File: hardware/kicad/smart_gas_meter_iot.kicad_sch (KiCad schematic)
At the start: 19 parts, among them J1 ESP32-S3-DEVKITC-1-J1, J2 ESP32-S3-DEVKITC-1-J2, J3 ESP-Prog-ProgramCOM-RECV, J4 USB2.0_C_v3, SW1 RS, SW2 BT, U1 ESP32-S3-WROOM-1, U2 AMS1117-3.3

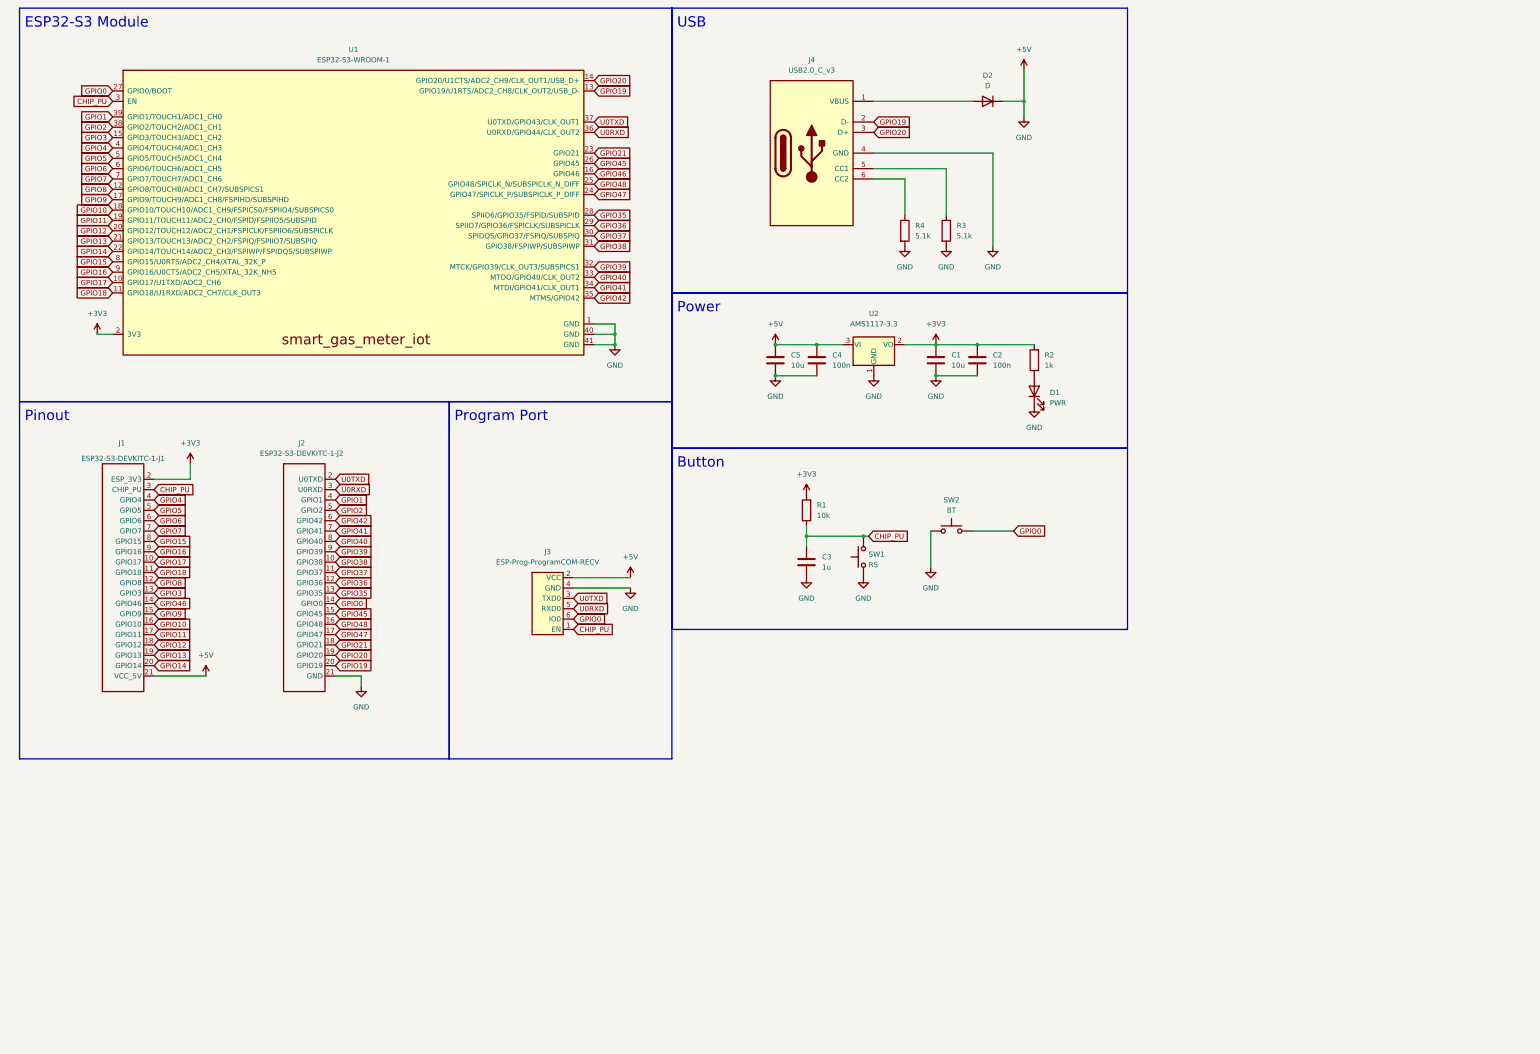
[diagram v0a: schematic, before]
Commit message: Rebuild v0.2 KiCad schematic from a reviewed design table (ERC clean)
Controlled rebuild per CONTROLLED_REBUILD_SPEC.md steps 1-5:
- Archive the frozen draft (65 ERC messages, +5V/GND short) as evidence.
- Add design_v02.py as the single source of truth (parts, values,
  footprints, pin-to-net map) and tools/generate_schematic.py to build
  the native schematic, project file and project-local SGM symbol and
  footprint libraries from it.
- Module-only carrier: USB-C with separate CC Rd, PTC + TVS, USBLC6 ESD,
  AP63203 buck (datasheet typical application), ESP32-S3-WROOM-1-N8 with
  EN RC and BOOT/RESET, synthetic pulse input on GPIO4, status LED,
  tamper input, I2C/UART headers, modem daughterboard connector with a
  separate MODEM_VIN, and test points.
- KiCad 9.0.3 ERC: 0 errors, 0 warnings, no exclusions.
- Add check_netlist_matches_design.py and run it in CAD CI together with
  a schematic/design sync check.
- Fix check_netlist_invariants.py: the net parser missed the last net and
  never read pinfunction, so GND-on-rail checks could not fire; identify
  legacy dev-board headers by library/part instead of J1/J2 refs; normalise
  local-label net names; add a modem-on-3V3 check. It now reports all 10
  faults of the archived draft.
- Export schematic PDF/PNG, ERC report, netlist and generated BOM.
- Add .gitignore; fix literal \n in README roadmaps.

Co-Authored-By: Claude Opus 5.5 <noreply@anthropic.com>
Claude-Session: https://claude.ai/code/session_01KogE8voCCVefmDU5WM67kg
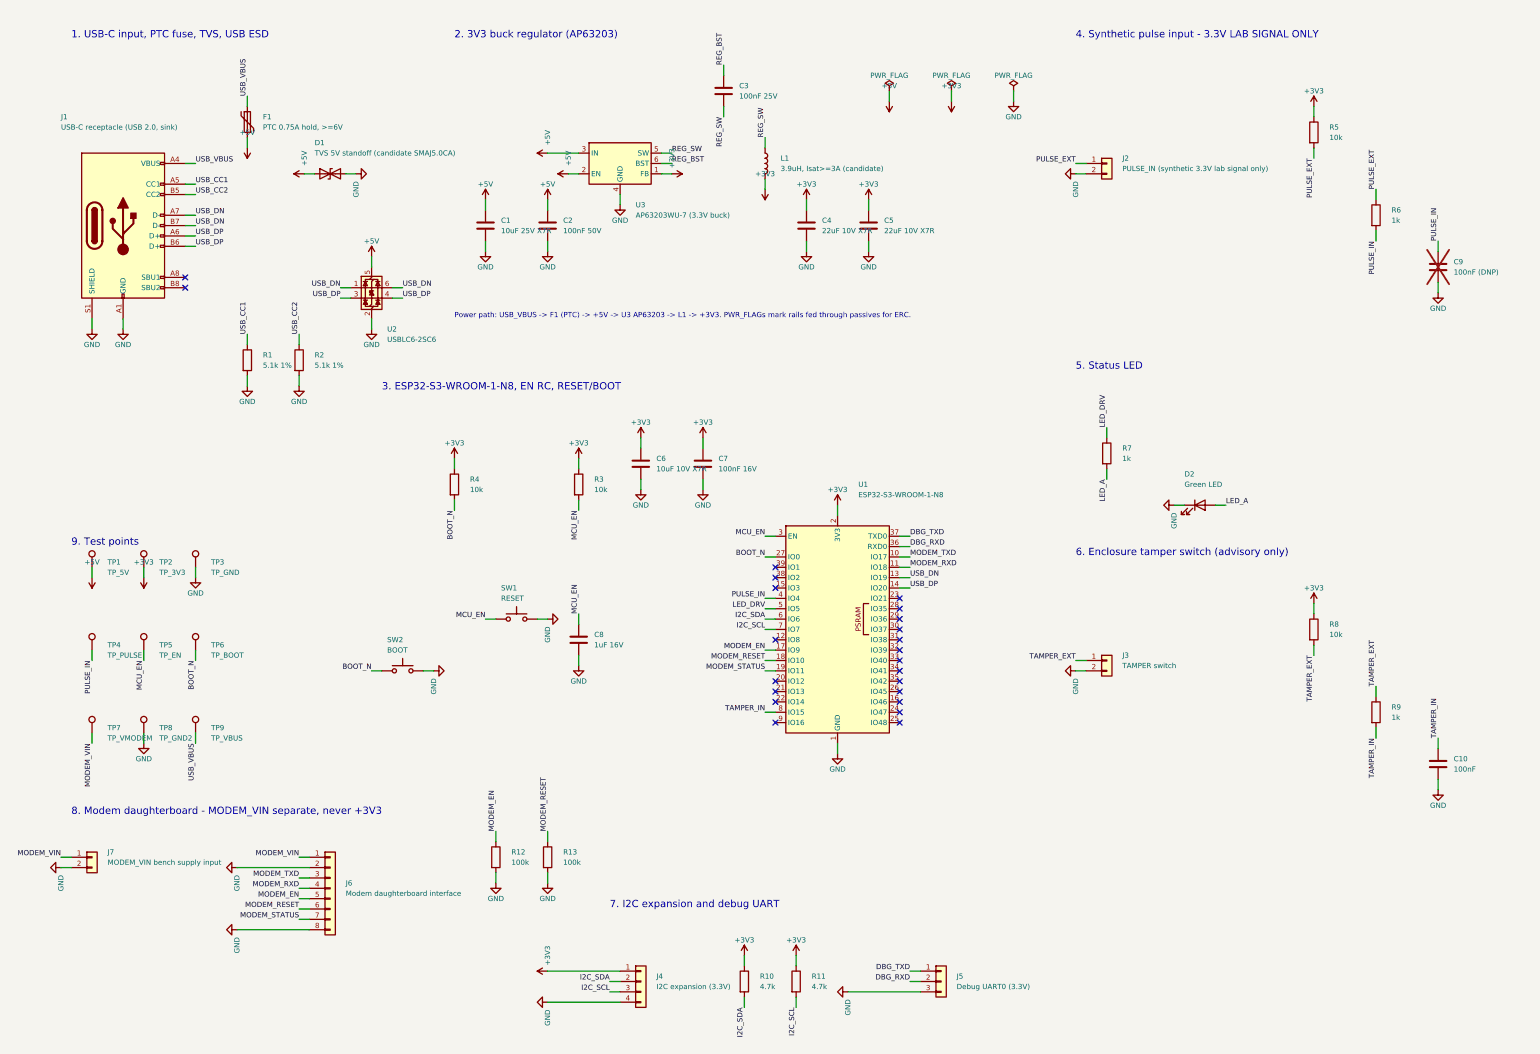
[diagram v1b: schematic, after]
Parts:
- removed C1, C5: 10u, esp32-dev-boards:Capacitor_0805_2012, symbol Device:C
- removed C2, C4: 100n, esp32-dev-boards:Capacitor_0805_2012, symbol Device:C
- removed C3: 1u, esp32-dev-boards:Capacitor_0805_2012, symbol Device:C
- removed D1: PWR, LED_SMD:LED_0805_2012Metric_Pad1.15x1.40mm_HandSolder, symbol Device:LED
- removed D2: D, Diode_SMD:D_SMA, symbol Device:D
- removed J1: ESP32-S3-DEVKITC-1-J1, esp32-dev-boards:ESP32-S3-DEVKITC-J1-mini, symbol esp32-dev-boards:ESP32-S3-DEVKITC-1-J1-mini
- removed J2: ESP32-S3-DEVKITC-1-J2, esp32-dev-boards:ESP32-S3-DEVKITC-J2-mini, symbol esp32-dev-boards:ESP32-S3-DEVKITC-1-J2-mini
- removed J3: ESP-Prog-ProgramCOM-RECV, $74th:BoxPinHeader_2x03_P1.27mm_Vertical, symbol $74th:ESP-Prog-ProgramCOM-RECV
- removed J4: USB2.0_C_v3, $74th:USB-C-12-Pin-SMD, symbol $74th:USB2.0_C_v3
- removed R1: 10k, esp32-dev-boards:Register_0805_2012, symbol Device:R
- removed R2: 1k, esp32-dev-boards:Register_0805_2012, symbol Device:R
- removed R3, R4: 5.1k, esp32-dev-boards:Register_0805_2012, symbol Device:R
- removed SW1: RS, esp32-dev-boards:SKRPABE010, symbol Switch:SW_Push
- removed SW2: BT, esp32-dev-boards:SKRPABE010, symbol Switch:SW_Push
- removed U1: ESP32-S3-WROOM-1, Espressif:ESP32-S3-WROOM-1, symbol Espressif:ESP32-S3-WROOM-1
- removed U2: AMS1117-3.3, Package_TO_SOT_SMD:SOT-223-3_TabPin2, symbol Regulator_Linear:AMS1117-3.3
- added C1: 10uF 25V X7R, SGM:C_1206_3216Metric, symbol SGM:C
- added C10: 100nF, SGM:C_0603_1608Metric, symbol SGM:C
- added C2: 100nF 50V, SGM:C_0603_1608Metric, symbol SGM:C
- added C3: 100nF 25V, SGM:C_0603_1608Metric, symbol SGM:C
- added C4, C5: 22uF 10V X7R, SGM:C_0805_2012Metric, symbol SGM:C
- added C6: 10uF 10V X7R, SGM:C_0805_2012Metric, symbol SGM:C
- added C7: 100nF 16V, SGM:C_0603_1608Metric, symbol SGM:C
- added C8: 1uF 16V, SGM:C_0603_1608Metric, symbol SGM:C
- added C9: 100nF (DNP), SGM:C_0603_1608Metric, symbol SGM:C
- added D1: TVS 5V standoff (candidate SMAJ5.0CA), SGM:D_SMA, symbol SGM:D_TVS
- added D2: Green LED, SGM:LED_0603_1608Metric, symbol SGM:LED
- added F1: PTC 0.75A hold, >=6V, SGM:Fuse_1206_3216Metric, symbol SGM:Polyfuse
- added J1: USB-C receptacle (USB 2.0, sink), SGM:USB_C_Receptacle_GCT_USB4105-xx-A_16P_TopMnt_Horizontal, symbol SGM:USB_C_Receptacle_USB2.0_16P
- added J2: PULSE_IN (synthetic 3.3V lab signal only), SGM:PinHeader_1x02_P2.54mm_Vertical, symbol SGM:Conn_01x02
- added J3: TAMPER switch, SGM:PinHeader_1x02_P2.54mm_Vertical, symbol SGM:Conn_01x02
- added J4: I2C expansion (3.3V), SGM:PinHeader_1x04_P2.54mm_Vertical, symbol SGM:Conn_01x04
- added J5: Debug UART0 (3.3V), SGM:PinHeader_1x03_P2.54mm_Vertical, symbol SGM:Conn_01x03
- added J6: Modem daughterboard interface, SGM:PinHeader_1x08_P2.54mm_Vertical, symbol SGM:Conn_01x08
- added J7: MODEM_VIN bench supply input, SGM:PinHeader_1x02_P2.54mm_Vertical, symbol SGM:Conn_01x02
- added L1: 3.9uH, Isat>=3A (candidate), SGM:L_Taiyo-Yuden_NR-40xx, symbol SGM:L
- added R1, R2: 5.1k 1%, SGM:R_0603_1608Metric, symbol SGM:R
- added R10, R11: 4.7k, SGM:R_0603_1608Metric, symbol SGM:R
- added R12, R13: 100k, SGM:R_0603_1608Metric, symbol SGM:R
- added R3, R4, R5, R8: 10k, SGM:R_0603_1608Metric, symbol SGM:R
- added R6, R7, R9: 1k, SGM:R_0603_1608Metric, symbol SGM:R
- added SW1: RESET, SGM:SW_SPST_TL3342, symbol SGM:SW_Push
- added SW2: BOOT, SGM:SW_SPST_TL3342, symbol SGM:SW_Push
- added TP1: TP_5V, SGM:TestPoint_Pad_D1.5mm, symbol SGM:TestPoint
- added TP2: TP_3V3, SGM:TestPoint_Pad_D1.5mm, symbol SGM:TestPoint
- added TP3: TP_GND, SGM:TestPoint_Pad_D1.5mm, symbol SGM:TestPoint
- added TP4: TP_PULSE, SGM:TestPoint_Pad_D1.5mm, symbol SGM:TestPoint
- added TP5: TP_EN, SGM:TestPoint_Pad_D1.5mm, symbol SGM:TestPoint
- added TP6: TP_BOOT, SGM:TestPoint_Pad_D1.5mm, symbol SGM:TestPoint
- added TP7: TP_VMODEM, SGM:TestPoint_Pad_D1.5mm, symbol SGM:TestPoint
- added TP8: TP_GND2, SGM:TestPoint_Pad_D1.5mm, symbol SGM:TestPoint
- added TP9: TP_VBUS, SGM:TestPoint_Pad_D1.5mm, symbol SGM:TestPoint
- added U1: ESP32-S3-WROOM-1-N8, SGM:ESP32-S3-WROOM-1, symbol SGM:ESP32-S3-WROOM-1
- added U2: USBLC6-2SC6, SGM:SOT-23-6, symbol SGM:USBLC6-2SC6
- added U3: AP63203WU-7 (3.3V buck), SGM:TSOT-23-6, symbol SGM:AP63203WU
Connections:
- net +3V3: now also C4.1, C5.1, C6.1, C7.1, J4.1 (Pin_1), L1.2, R10.1, R11.1, R3.1, R4.1, R5.1, R8.1, TP2.1, U1.2 (3V3), U3.1 (FB)
- net +5V: now also C1.1, C2.1, D1.1 (A1), F1.2, TP1.1, U2.5 (VBUS), U3.2 (EN), U3.3 (IN)
- new net BOOT_N: R4.2, SW2.1, TP6.1, U1.27 (IO0)
- new net DBG_RXD: J5.2 (Pin_2), U1.36 (RXD0)
- new net DBG_TXD: J5.1 (Pin_1), U1.37 (TXD0)
- new net GND: C1.2, C10.2, C2.2, C4.2, C5.2, C6.2, C7.2, C8.2, C9.2, D1.2 (A2), D2.1 (K), J1.A1 (GND), J1.A12 (GND), J1.B1 (GND), J1.B12 (GND), J1.S1 (SHIELD), J2.2 (Pin_2), J3.2 (Pin_2), J4.4 (Pin_4), J5.3 (Pin_3), J6.2 (Pin_2), J6.8 (Pin_8), J7.2 (Pin_2), R1.2, R12.2, R13.2, R2.2, SW1.2, SW2.2, TP3.1, TP8.1, U1.1 (GND), U1.40 (GND), U1.41 (GND), U2.2 (GND), U3.4 (GND)
- new net I2C_SCL: J4.3 (Pin_3), R11.2, U1.7 (IO7)
- new net I2C_SDA: J4.2 (Pin_2), R10.2, U1.6 (IO6)
- new net LED_A: D2.2 (A), R7.2
- new net LED_DRV: R7.1, U1.5 (IO5)
- new net MCU_EN: C8.1, R3.2, SW1.1, TP5.1, U1.3 (EN)
- new net MODEM_EN: J6.5 (Pin_5), R12.1, U1.17 (IO9)
- new net MODEM_RESET: J6.6 (Pin_6), R13.1, U1.18 (IO10)
- new net MODEM_RXD: J6.4 (Pin_4), U1.11 (IO18)
- new net MODEM_STATUS: J6.7 (Pin_7), U1.19 (IO11)
- new net MODEM_TXD: J6.3 (Pin_3), U1.10 (IO17)
- new net MODEM_VIN: J6.1 (Pin_1), J7.1 (Pin_1), TP7.1
- new net PULSE_EXT: J2.1 (Pin_1), R5.2, R6.1
- new net PULSE_IN: C9.1, R6.2, TP4.1, U1.4 (IO4)
- new net REG_BST: C3.1, U3.6 (BST)
- new net REG_SW: C3.2, L1.1, U3.5 (SW)
- new net TAMPER_EXT: J3.1 (Pin_1), R8.2, R9.1
- new net TAMPER_IN: C10.1, R9.2, U1.8 (IO15)
- new net USB_CC1: J1.A5 (CC1), R1.1
- new net USB_CC2: J1.B5 (CC2), R2.1
- new net USB_DN: J1.A7 (D-), J1.B7 (D-), U1.13 (IO19), U2.1 (I/O1), U2.6 (I/O1)
- new net USB_DP: J1.A6 (D+), J1.B6 (D+), U1.14 (IO20), U2.3 (I/O2), U2.4 (I/O2)
- new net USB_VBUS: F1.1, J1.A4 (VBUS), J1.A9 (VBUS), J1.B4 (VBUS), J1.B9 (VBUS), TP9.1
- no-connect marks 0 -> 23
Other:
- note added: "1. USB-C input, PTC fuse, TVS, USB ESD"
- note added: "2. 3V3 buck regulator (AP63203)"
- note added: "3. ESP32-S3-WROOM-1-N8, EN RC, RESET/BOOT"
- note added: "4. Synthetic pulse input - 3.3V LAB SIGNAL ONLY"
- note added: "5. Status LED"
- note added: "6. Enclosure tamper switch (advisory only)"
- note added: "7. I2C expansion and debug UART"
- note added: "8. Modem daughterboard - MODEM_VIN separate, never +3V3"
- note added: "9. Test points"
- note added: "Power path: USB_VBUS -> F1 (PTC) -> +5V -> U3 AP63203 -> L1 -> +3V3. PWR_FLAGs mark rails fed through passives for ERC."
- note removed: "Button"
- note removed: "ESP32-S3 Module"
- note removed: "Pinout"
- note removed: "Power"
- note removed: "Program Port"
- note removed: "USB"
- company: Smart Gas Meter IoT -> Smart Gas Meter IoT - lab prototype
- title: Smart Gas Meter IoT — ESP32-S3 carrier draft -> Smart Gas Meter IoT - carrier board v0.2 (controlled rebuild)

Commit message: Select exact parts and freeze schematic candidate v0.2-rc1
- Record orderable MPN + LCSC code for every assembled part in
  design_v02.py (PART_SELECTION) and emit MPN/Manufacturer/LCSC fields
  into the schematic.
- Ratings checked against datasheets/parametric data; documented in
  PART_SELECTION.md with a load budget. Notable corrections:
  * PTC: 1206L075/13.2WR (13.2 V), not the lower-voltage THYR variant.
  * TVS: SMAJ6.5CA instead of a 5.0 V stand-off part on a USB 5 V rail.
  * Status LED: red (Vf 2.0-2.4 V); the green candidate had Vf ~3.3 V.
  * Output caps 22 uF 16 V for less DC-bias loss; inductor Sunlord
    SWPA4030S3R9MT (3.9 uH, Isat 3 A) with its dedicated footprint.
- Add tools/export_bom.py (review BOM + JLCPCB assembly CSV) and tests
  for selection completeness and BOM sync.
- KiCad 9.0.3 ERC: 0 errors, 0 warnings; netlist matches design.
- Freeze checklist updated with evidence; land-pattern overlay and
  second-engineer sign-off remain open.

Co-Authored-By: Claude Opus 5.5 <noreply@anthropic.com>
Claude-Session: https://claude.ai/code/session_01KogE8voCCVefmDU5WM67kg
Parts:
- C1: LCSC (none) -> C77093; MPN TBD -> GRM31CR71E106KA12L; Manufacturer (none) -> Murata
- C10: value 100nF -> 100nF 50V; LCSC (none) -> C14663; MPN TBD -> CC0603KRX7R9BB104; Manufacturer (none) -> YAGEO
- C2: LCSC (none) -> C14663; MPN TBD -> CC0603KRX7R9BB104; Manufacturer (none) -> YAGEO
- C3: value 100nF 25V -> 100nF 50V; LCSC (none) -> C14663; MPN TBD -> CC0603KRX7R9BB104; Manufacturer (none) -> YAGEO
- C4, C5: value 22uF 10V X7R -> 22uF 16V; LCSC (none) -> C86817; MPN TBD -> GRM21BR61C226ME44L; Manufacturer (none) -> Murata
- C6: value 10uF 10V X7R -> 10uF 25V; LCSC (none) -> C15850; MPN TBD -> CL21A106KAYNNNE; Manufacturer (none) -> Samsung
- C7: value 100nF 16V -> 100nF 50V; LCSC (none) -> C14663; MPN TBD -> CC0603KRX7R9BB104; Manufacturer (none) -> YAGEO
- C8: value 1uF 16V -> 1uF 50V; LCSC (none) -> C15849; MPN TBD -> CL10A105KB8NNNC; Manufacturer (none) -> Samsung
- C9: value 100nF (DNP) -> 100nF 50V (DNP); LCSC (none) -> C14663; MPN TBD -> CC0603KRX7R9BB104; Manufacturer (none) -> YAGEO
- D1: value TVS 5V standoff (candidate SMAJ5.0CA) -> SMAJ6.5CA; LCSC (none) -> C5161320; MPN SMAJ5.0CA (candidate) -> SMAJ6.5CA; Manufacturer (none) -> ZHIDE
- D2: value Green LED -> Red LED; LCSC (none) -> C2986056; MPN TBD -> 19-213SURC/S530-A3/5T; Manufacturer (none) -> Everlight
- F1: value PTC 0.75A hold, >=6V -> PTC 0.75A/13.2V; LCSC (none) -> C207036; MPN TBD -> 1206L075/13.2WR; Manufacturer (none) -> Littelfuse
- J1: value USB-C receptacle (USB 2.0, sink) -> USB4105-GF-A (USB-C); LCSC (none) -> C3020560; MPN GCT USB4105-GF-A (candidate) -> USB4105-GF-A; Manufacturer (none) -> GCT
- J2, J3, J4, J5, J6, J7, TP1, TP2, TP3, TP4, TP5, TP6, TP7, TP8, TP9: MPN TBD -> generic
- L1: value 3.9uH, Isat>=3A (candidate) -> 3.9uH Isat 3A; footprint SGM:L_Taiyo-Yuden_NR-40xx -> SGM:L_Sunlord_SWPA4030S; LCSC (none) -> C96899; MPN TBD -> SWPA4030S3R9MT; Manufacturer (none) -> Sunlord
- R1, R2: LCSC (none) -> C23186; MPN TBD -> 0603WAF5101T5E; Manufacturer (none) -> UNI-ROYAL
- R10, R11: value 4.7k -> 4.7k 1%; LCSC (none) -> C23162; MPN TBD -> 0603WAF4701T5E; Manufacturer (none) -> UNI-ROYAL
- R12, R13: value 100k -> 100k 1%; LCSC (none) -> C25803; MPN TBD -> 0603WAF1003T5E; Manufacturer (none) -> UNI-ROYAL
- R3, R4, R5, R8: value 10k -> 10k 1%; LCSC (none) -> C25804; MPN TBD -> 0603WAF1002T5E; Manufacturer (none) -> UNI-ROYAL
- R6, R7, R9: value 1k -> 1k 1%; LCSC (none) -> C21190; MPN TBD -> 0603WAF1001T5E; Manufacturer (none) -> UNI-ROYAL
- SW1: value RESET -> TL3342; LCSC (none) -> C2886898; MPN TBD -> TL3342F160QG; Manufacturer (none) -> E-Switch
- SW2: value BOOT -> TL3342; LCSC (none) -> C2886898; MPN TBD -> TL3342F160QG; Manufacturer (none) -> E-Switch
- U1: LCSC (none) -> C2913198; MPN Espressif ESP32-S3-WROOM-1-N8 -> ESP32-S3-WROOM-1-N8; Manufacturer (none) -> Espressif
- U2: LCSC (none) -> C7519; MPN STMicroelectronics USBLC6-2SC6 -> USBLC6-2SC6; Manufacturer (none) -> STMicroelectronics
- U3: value AP63203WU-7 (3.3V buck) -> AP63203WU-7; LCSC (none) -> C780769; MPN Diodes Inc. AP63203WU-7 -> AP63203WU-7; Manufacturer (none) -> Diodes Inc.

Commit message: Route the 4-layer v0.2 carrier PCB (DRC clean, schematic parity)
- Committed routed board smart_gas_meter_iot.kicad_pcb: 100 x 70 mm,
  F.Cu signals / In1 solid GND / In2 signals + 3V3 pour / B.Cu signals,
  48 vias (29 GND fan-out), autorouted with Freerouting 2.1.
- KiCad 9.0.3 DRC (all severities, --schematic-parity): 0 violations,
  0 unconnected pads, 0 parity issues. Schematic ERC 0/0.
- Unconnected pins carry KiCad's per-pin unconnected-(...) nets; test
  points are excluded from the BOM in the schematic too.
- B.Cu GND pour dropped (single-spoke header thermals, islands); In1 is
  the solid reference. Rotate-angle syntax fixed in export_pcb.sh.
- exports/pcb: DRC report, Gerbers + drill + map, CPL, layer PDFs and
  CAD-derived 3D renders (review artefacts only).
- PCB_DESIGN.md documents stack-up, placement rationale, how the board
  is produced, verification and the open review items (USB pair tuning,
  power-loop review, land-pattern overlay, DFM, sign-off). README,
  rebuild spec, freeze/board-gate checklists updated.

Co-Authored-By: Claude Opus 5.5 <noreply@anthropic.com>
Claude-Session: https://claude.ai/code/session_01KogE8voCCVefmDU5WM67kg
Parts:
- TP1, TP2, TP3, TP4, TP5, TP6, TP7, TP8, TP9: now left out of the parts list
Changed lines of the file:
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@@
   )
   (symbol (lib_id "SGM:TestPoint") (at 30.48 149.86 0) (unit 1)
-    (in_bom yes) (on_board yes) (dnp no)
+    (in_bom no) (on_board yes) (dnp no)
     (property "Reference" "TP1" (at 34.29 148.59 0)
       (effects (font (size 1.27 1.27)) (justify left))
@@
   )
   (symbol (lib_id "SGM:TestPoint") (at 43.18 149.86 0) (unit 1)
-    (in_bom yes) (on_board yes) (dnp no)
+    (in_bom no) (on_board yes) (dnp no)
     (property "Reference" "TP2" (at 46.99 148.59 0)
       (effects (font (size 1.27 1.27)) (justify left))
@@
   )
   (symbol (lib_id "SGM:TestPoint") (at 55.88 149.86 0) (unit 1)
-    (in_bom yes) (on_board yes) (dnp no)
+    (in_bom no) (on_board yes) (dnp no)
     (property "Reference" "TP3" (at 59.69 148.59 0)
       (effects (font (size 1.27 1.27)) (justify left))
@@
   )
   (symbol (lib_id "SGM:TestPoint") (at 30.48 170.18 0) (unit 1)
-    (in_bom yes) (on_board yes) (dnp no)
+    (in_bom no) (on_board yes) (dnp no)
     (property "Reference" "TP4" (at 34.29 168.91 0)
       (effects (font (size 1.27 1.27)) (justify left))
@@
   )
   (symbol (lib_id "SGM:TestPoint") (at 43.18 170.18 0) (unit 1)
-    (in_bom yes) (on_board yes) (dnp no)
+    (in_bom no) (on_board yes) (dnp no)
     (property "Reference" "TP5" (at 46.99 168.91 0)
       (effects (font (size 1.27 1.27)) (justify left))
@@
   )
   (symbol (lib_id "SGM:TestPoint") (at 55.88 170.18 0) (unit 1)
-    (in_bom yes) (on_board yes) (dnp no)
+    (in_bom no) (on_board yes) (dnp no)
     (property "Reference" "TP6" (at 59.69 168.91 0)
       (effects (font (size 1.27 1.27)) (justify left))
@@
   )
   (symbol (lib_id "SGM:TestPoint") (at 30.48 190.5 0) (unit 1)
-    (in_bom yes) (on_board yes) (dnp no)
+    (in_bom no) (on_board yes) (dnp no)
     (property "Reference" "TP7" (at 34.29 189.23 0)
       (effects (font (size 1.27 1.27)) (justify left))
@@
   )
   (symbol (lib_id "SGM:TestPoint") (at 43.18 190.5 0) (unit 1)
-    (in_bom yes) (on_board yes) (dnp no)
+    (in_bom no) (on_board yes) (dnp no)
     (property "Reference" "TP8" (at 46.99 189.23 0)
       (effects (font (size 1.27 1.27)) (justify left))
@@
   )
   (symbol (lib_id "SGM:TestPoint") (at 55.88 190.5 0) (unit 1)
-    (in_bom yes) (on_board yes) (dnp no)
+    (in_bom no) (on_board yes) (dnp no)
     (property "Reference" "TP9" (at 59.69 189.23 0)
       (effects (font (size 1.27 1.27)) (justify left))
